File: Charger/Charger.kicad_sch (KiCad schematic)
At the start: 27 parts, among them J1 PL00X-301-10M8, J2 PL00Y-301-10M8, K1 Gigavc PNC11BDA, K2 EV200 HAANA, SW1 Emergency Button, SW2 SW_Push, SW3 SW_Push, U1 ATmega328-A, Y1 20MHz

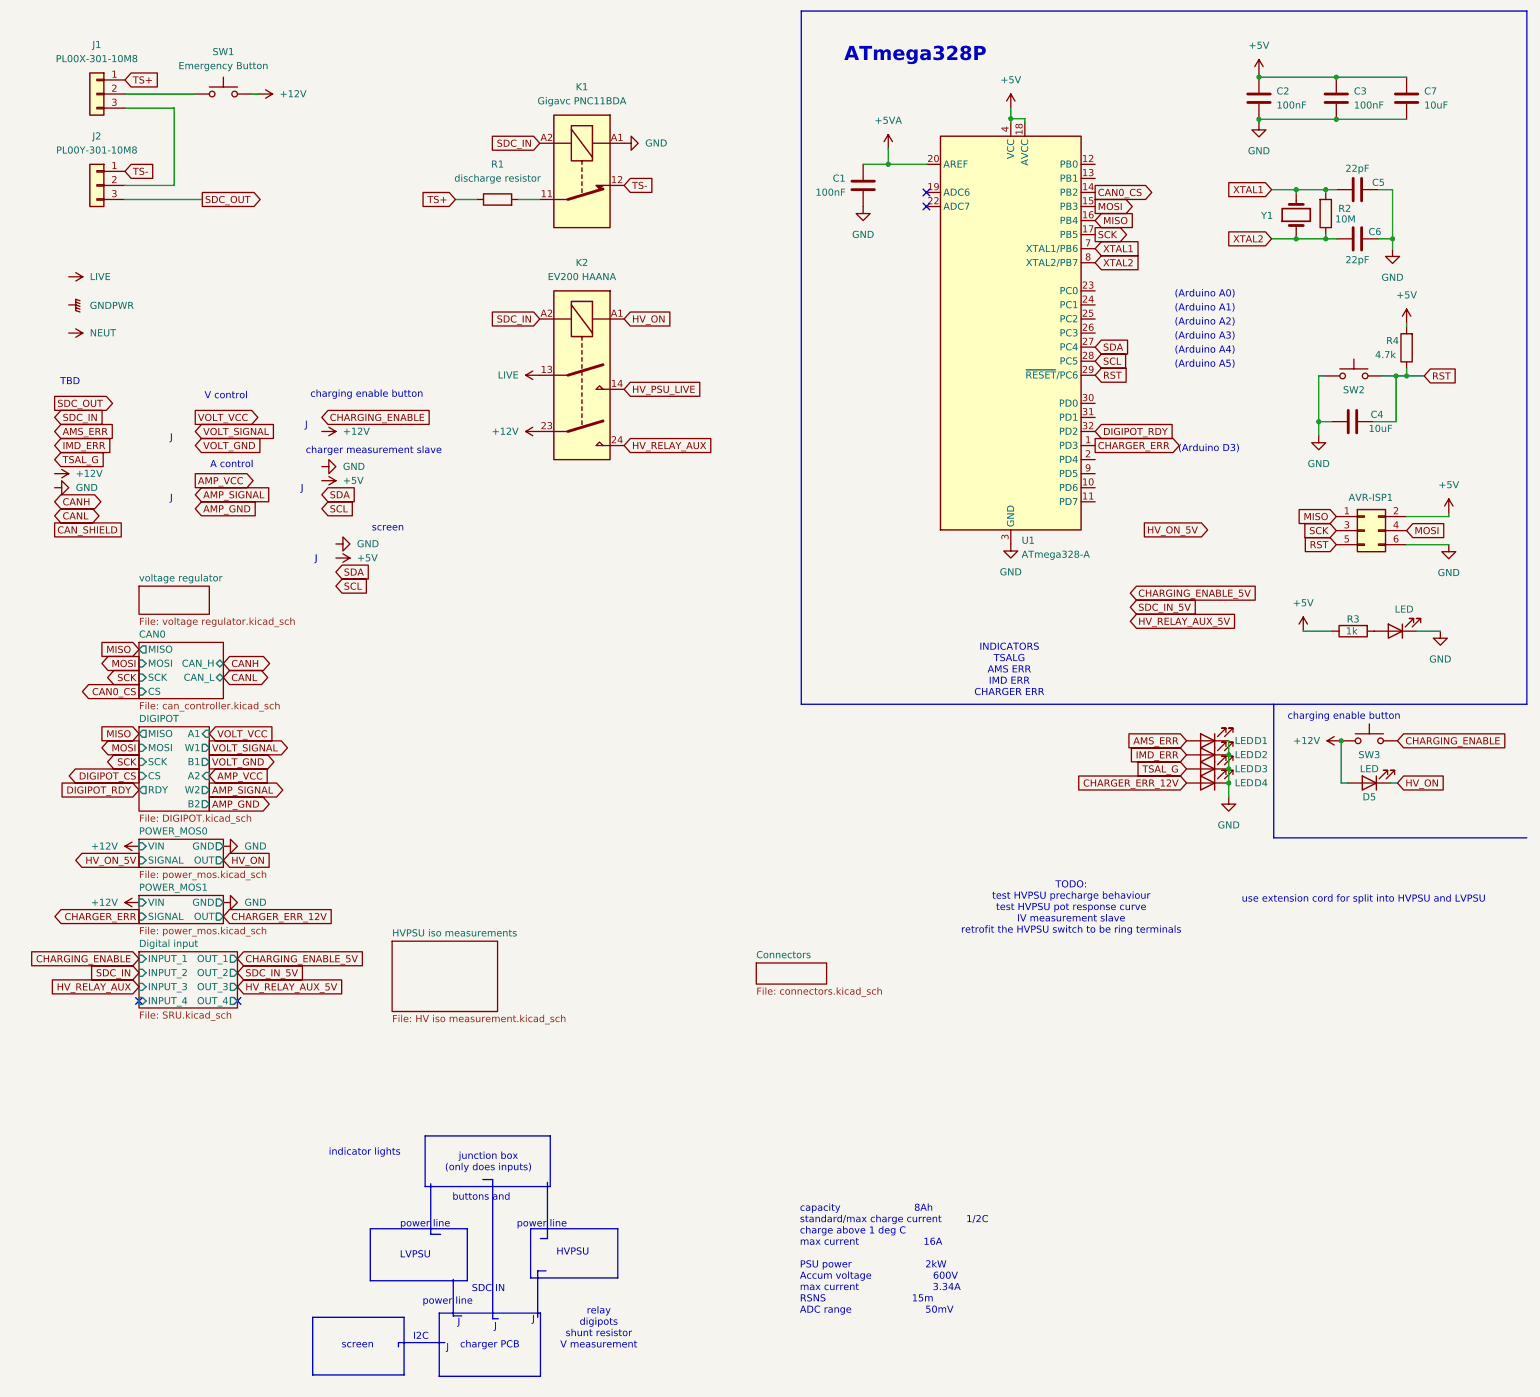
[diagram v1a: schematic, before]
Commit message: charger WIP
Most footprints assigned, shunt drawn in schem
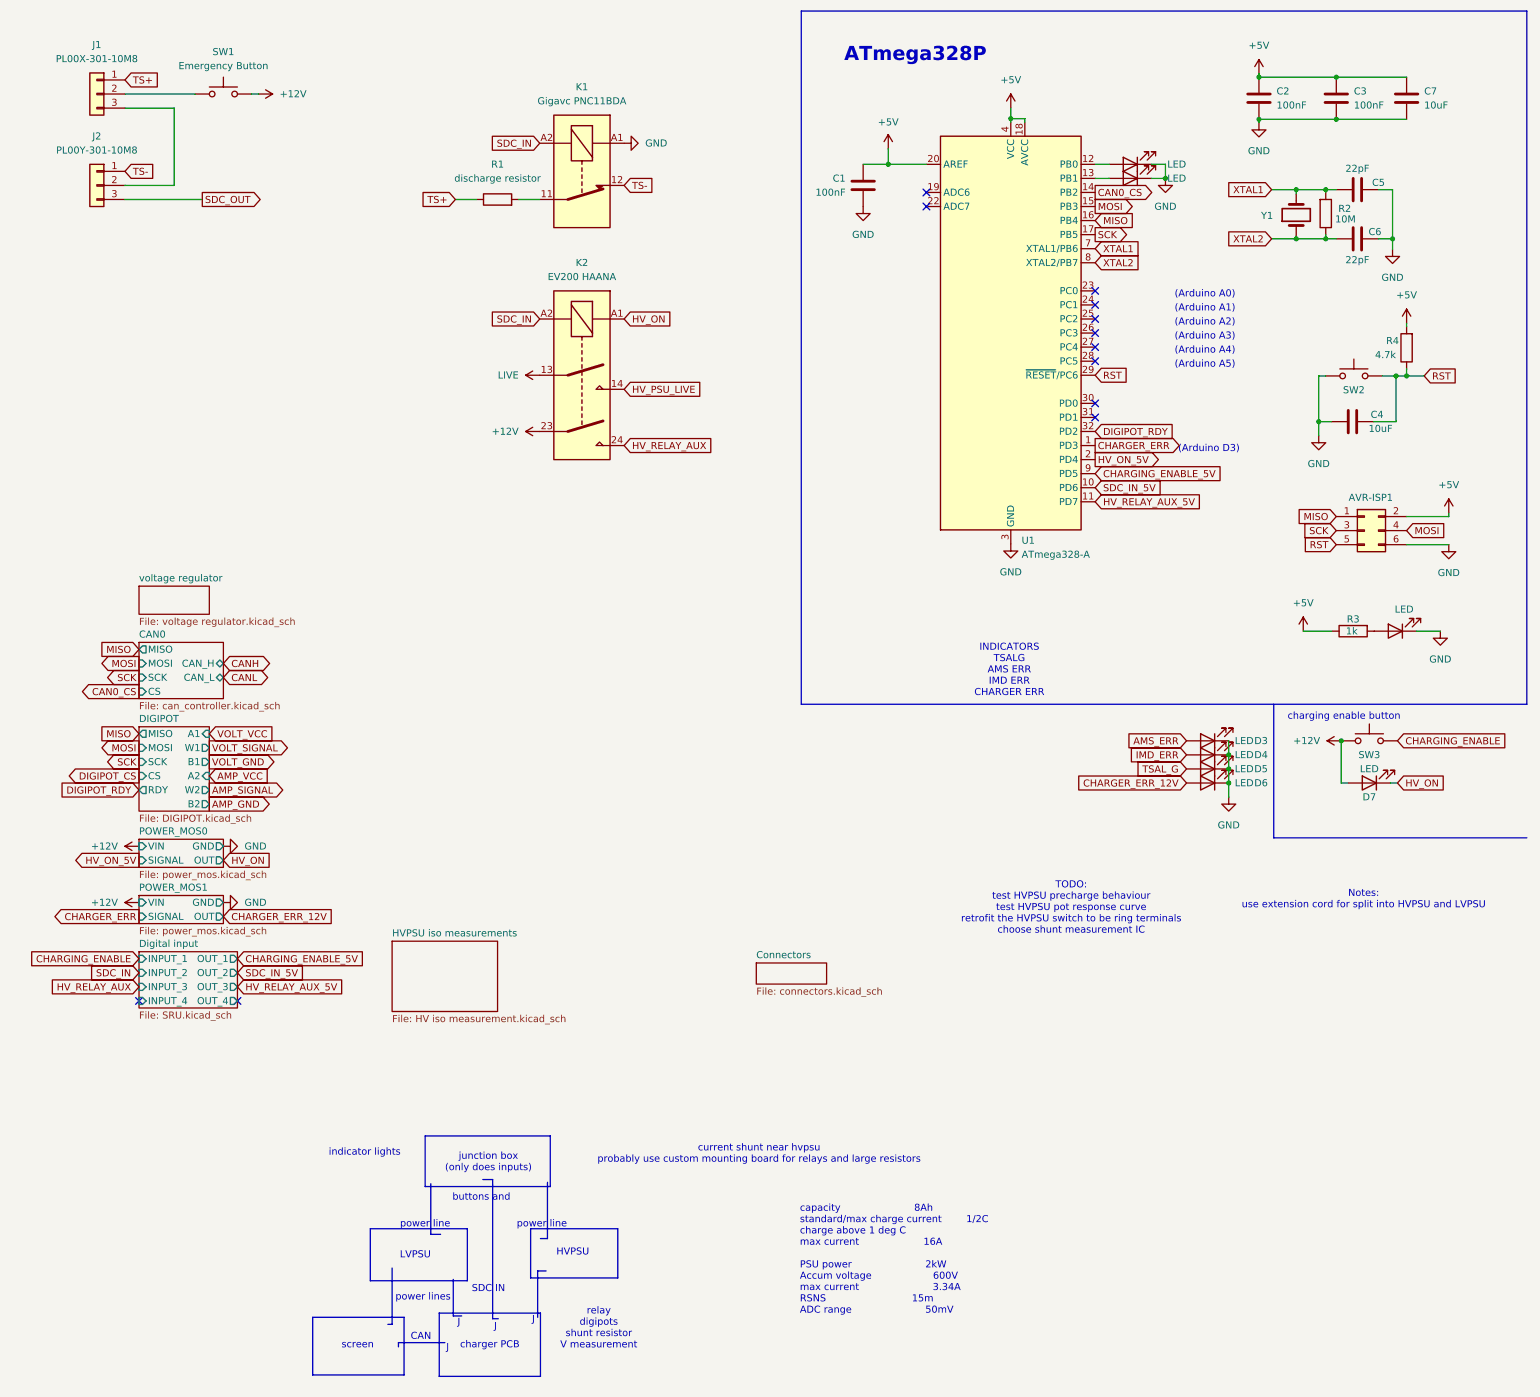
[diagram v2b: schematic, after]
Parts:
- added D1, D2: LED, RMC_LED:LED_0805_2012Metric_Pad1.45x1.40mm_HandSolder, symbol Device:LED
- renumbered D1 to D3, D2 to D4, D3 to D5, D4 to D6, D5 to D7, D6 to D8
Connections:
- net +5VA is gone; now on net +5V: C1.2, U1.20 (AREF)
- net CHARGING_ENABLE_5V: now also U1.9 (PD5)
- net GND: now also D1.1 (K), D2.1 (K)
- net HV_ON_5V: now also U1.2 (PD4)
- net HV_RELAY_AUX_5V: now also U1.11 (PD7)
- net SDC_IN_5V: now also U1.10 (PD6)
- net at U1.12 (PB0): now also D1.2 (A)
- net at U1.13 (PB1): now also D2.2 (A)
- net SCL: no longer names the net of U1.28 (PC5)
- net SDA: no longer names the net of U1.27 (PC4)
- no-connect marks 4 -> 12
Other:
- note added: "CAN"
- note added: "Notes: use extension cord for split into HVPSU and LVPSU"
- note added: "TODO: test HVPSU precharge behaviour test HVPSU pot response curve retrofit the HVPSU switch to be ring terminals choose shunt measurement IC"
- note added: "current shunt near hvpsu probably use custom mounting board for relays and large resistors"
- note added: "power lines"
- note removed: "A control"
- note removed: "I2C"
- note removed: "TBD"
- note removed: "TODO: test HVPSU precharge behaviour test HVPSU pot response curve IV measurement slave retrofit the HVPSU switch to be ring terminals"
- note removed: "V control"
- note removed: "charger measurement slave"
- note removed: "use extension cord for split into HVPSU and LVPSU"
